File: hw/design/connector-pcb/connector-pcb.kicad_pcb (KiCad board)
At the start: 2 copper layers, 20 x 20 mm, 5 parts, among them J1 B04B-JWPF-SK-R, J2 PinHeader (2.54mm), SW1 KSC421G70

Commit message: Final hardware design
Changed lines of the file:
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@@
       (outputformat 1)
       (mirror false)
-      (drillshape 1)
+      (drillshape 0)
       (scaleselection 1)
-      (outputdirectory "")
+      (outputdirectory "../../../../ordering-2024-05/connector-pcb/")
     )
   )
@@
       (stroke (width 0.1) (type solid)) (layer "F.Fab"))
     (pad "" np_thru_hole circle (at -1.5 8.05 270) (size 1.15 1.15) (drill 1.15) (layers "*.Cu" "*.Mask"))
-    (pad "1" thru_hole roundrect (at 0 0 270) (size 2 1.3) (drill 1) (layers "*.Cu" "*.Mask") (roundrect_rratio 0.192308)
+    (pad "1" thru_hole roundrect (at 0 0 270) (size 2 1.3) (drill 1) (layers "*.Cu" "*.Mask") (roundrect_rratio 0.1923076923)
       (net 1 "/VBAT") (pinfunction "Pin_1") (pintype "passive"))
     (pad "2" thru_hole oval (at 0 2 270) (size 2 1.3) (drill 1) (layers "*.Cu" "*.Mask")

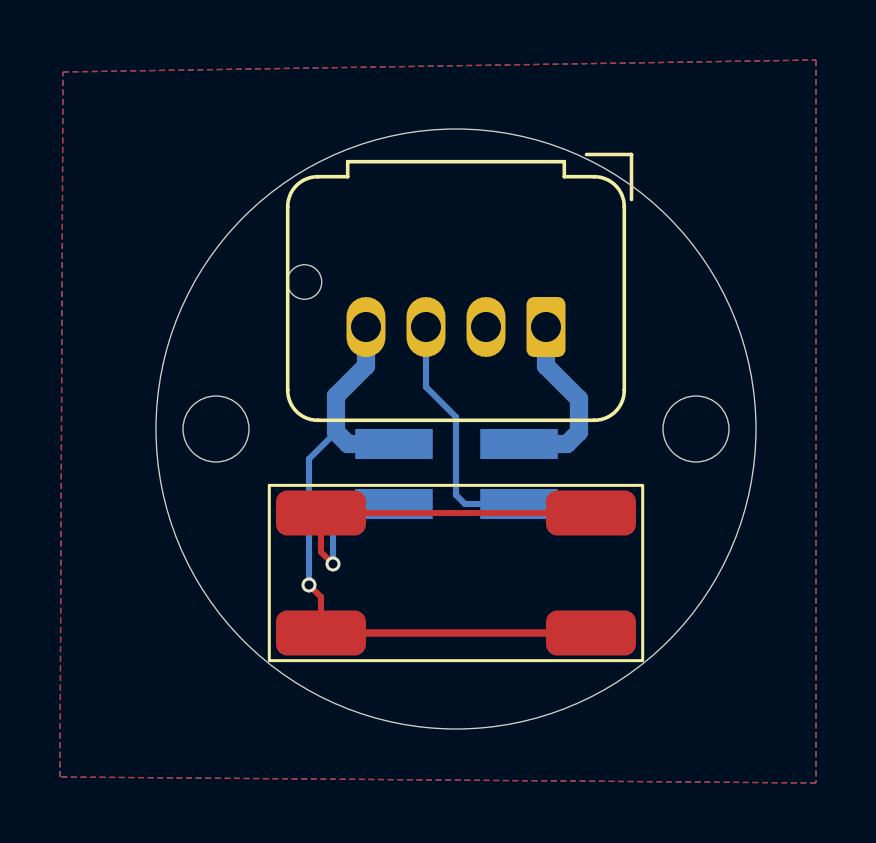
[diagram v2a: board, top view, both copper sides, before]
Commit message: Connector board modified to use the 3pin connector
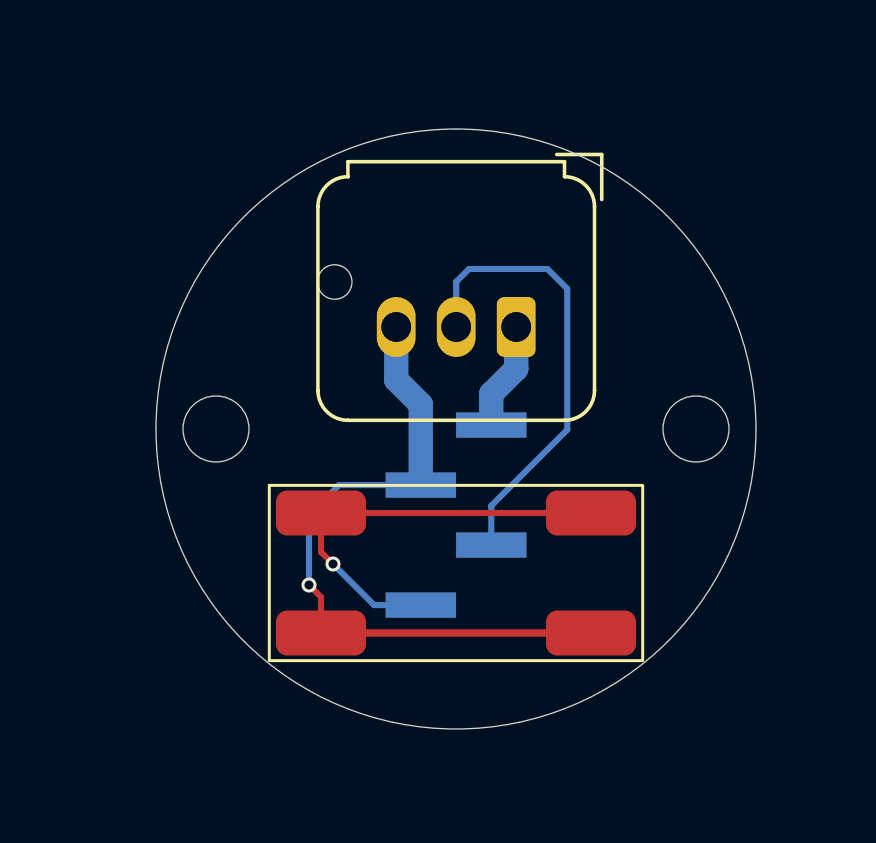
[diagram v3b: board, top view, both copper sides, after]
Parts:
- J1: value B04B-JWPF-SK-R -> B03B-JWPF-SK-R; footprint Connector_JST:JST_JWPF_B04B-JWPF-SK-R_1x04_P2.00mm_Vertical -> Connector_JST:JST_JWPF_B03B-JWPF-SK-R_1x03_P2.00mm_Vertical
- J2: footprint Connector_PinHeader_2.00mm:PinHeader_2x02_P2.00mm_Vertical_SMD -> Connector_PinHeader_2.00mm:PinHeader_1x04_P2.00mm_Vertical_SMD_Pin1Left
- moved J2 1.37 mm to (165.0, 114.8)
- moved J1 0.99 mm to (167.0, 108.5)
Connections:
- J1 pad 2: unconnected-(J1-Pin_2-Pad2) -> /LINE
- J1 pad 3: /LINE -> GND
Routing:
- net /LINE: track 8.24 -> 15.3 mm
- net /VBAT: track 6.12 -> 3.61 mm
- net GND: track 22.2 -> 22.8 mm
- removed copper zone on B.Cu, net (none)
- removed copper zone on F.Cu, net (none)
